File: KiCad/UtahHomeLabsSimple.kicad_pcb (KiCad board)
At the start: 2 copper layers, 20.3 x 20.3 mm, 5 parts, among them X1 SAINTCON-Minibadge-Simple

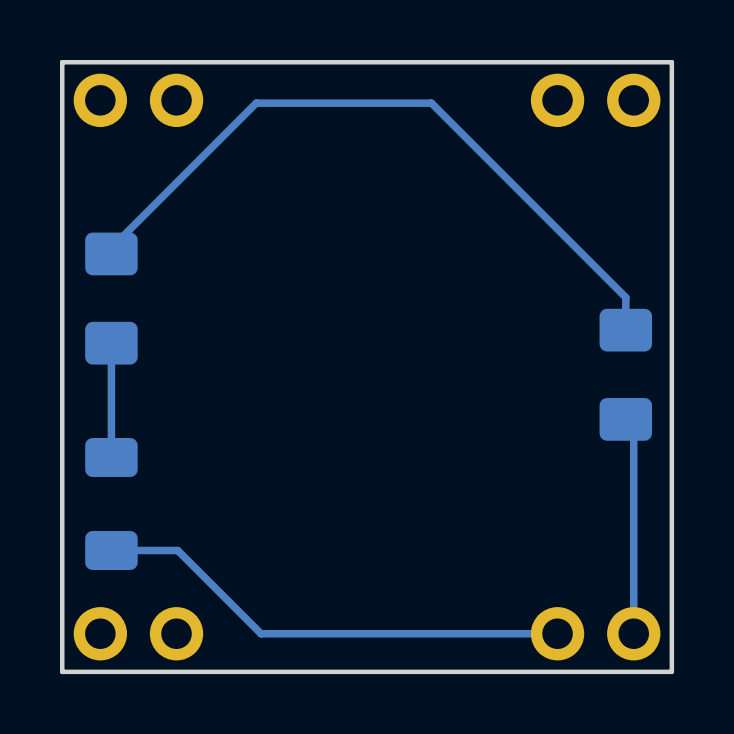
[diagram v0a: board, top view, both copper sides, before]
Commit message: Updates
Updated Schema to Parallel
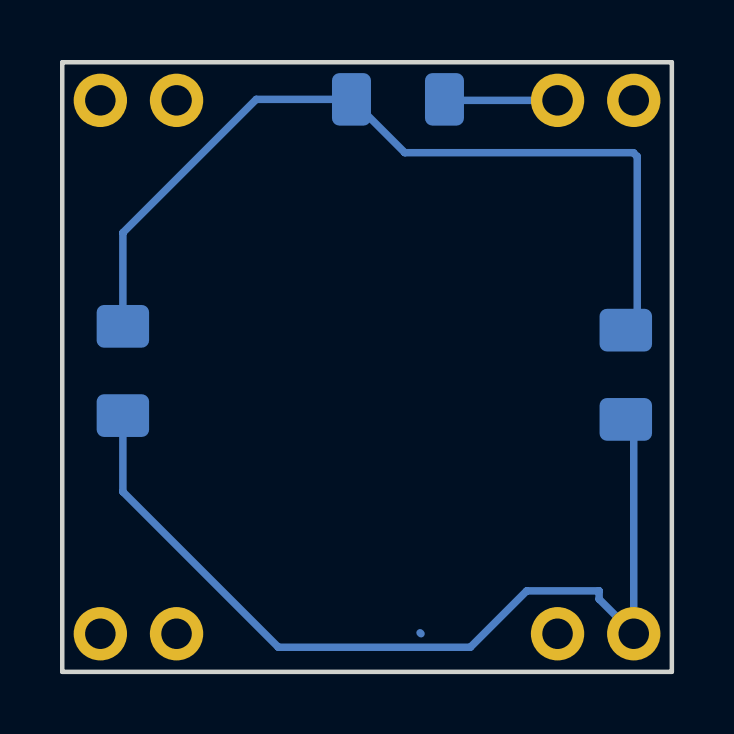
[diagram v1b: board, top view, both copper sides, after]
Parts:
- moved R1 16.5 mm to (137.2, 85.9), turned to 180 degrees
- moved D1 2.44 mm to (128.0, 94.9), turned to 90 degrees
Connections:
- D1 pad 2: Net-(D1-Pad2) -> Net-(D2-Pad2)
- D2 pad 1: Net-(X1-Pad16) -> Net-(D1-Pad1)
- D2 pad 2: Net-(D1-Pad1) -> Net-(D2-Pad2)
- R1 pad 2: Net-(D1-Pad2) -> Net-(D2-Pad2)
- X1 pad 15: Net-(R1-Pad1) -> unconnected-(X1-Pad15)
- X1 pad 16: Net-(X1-Pad16) -> Net-(D1-Pad1)
- X1 pad 7: unconnected-(X1-Pad7) -> Net-(R1-Pad1)
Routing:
- net Net-(D2-Pad2): track 0.00 -> 28.8 mm
- net Net-(R1-Pad1): track 16.0 -> 3.78 mm
- net Net-(D1-Pad1): track 23.1 -> 30.5 mm
- net Net-(X1-Pad16): track 7.25 -> 0.00 mm
- net Net-(D1-Pad2): track 3.81 -> 0.00 mm

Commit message: Re-did traces
Traces re-done
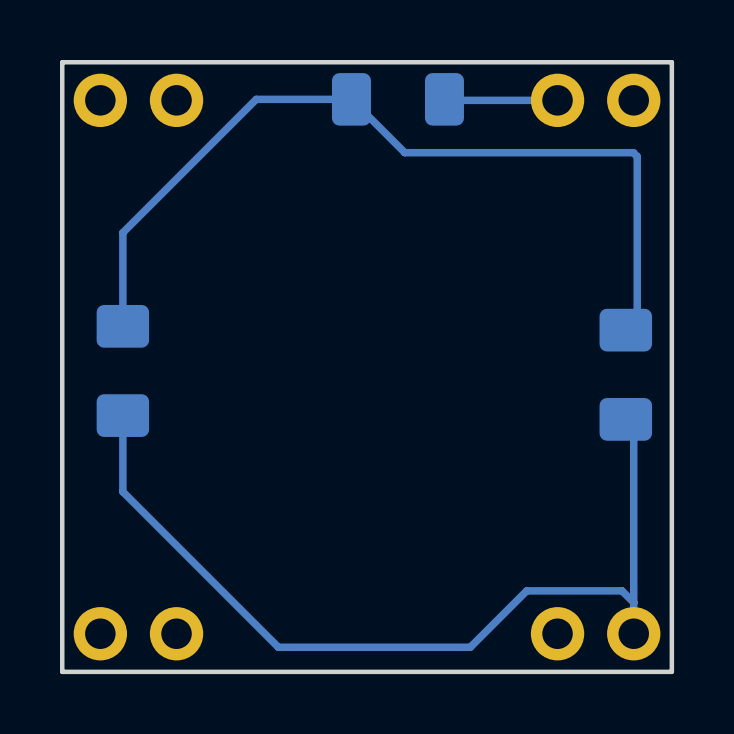
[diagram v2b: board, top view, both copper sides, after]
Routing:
- net Net-(D1-Pad1): track 30.5 -> 29.9 mm
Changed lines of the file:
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@@
     )
   )
-  (segment (start 137.955 103.665) (end 137.922 103.632) (width 0.25) (layer "B.Cu") (net 0))
   (segment (start 133.198 104.115) (end 139.598 104.115) (width 0.25) (layer "B.Cu") (net 1))
-  (segment (start 143.891 102.235) (end 143.891 102.511) (width 0.25) (layer "B.Cu") (net 1))
+  (segment (start 141.478 102.235) (end 144.653 102.235) (width 0.25) (layer "B.Cu") (net 1))
+  (segment (start 128.016 96.393) (end 128.016 98.933) (width 0.25) (layer "B.Cu") (net 1))
+  (segment (start 145.045 102.627) (end 145.045 103.665) (width 0.25) (layer "B.Cu") (net 1))
+  (segment (start 144.653 102.235) (end 145.045 102.627) (width 0.25) (layer "B.Cu") (net 1))
+  (segment (start 144.78 96.52) (end 145.045 96.785) (width 0.25) (layer "B.Cu") (net 1))
+  (segment (start 128.016 98.933) (end 133.198 104.115) (width 0.25) (layer "B.Cu") (net 1))
   (segment (start 139.598 104.115) (end 141.478 102.235) (width 0.25) (layer "B.Cu") (net 1))
-  (segment (start 144.78 96.52) (end 145.045 96.785) (width 0.25) (layer "B.Cu") (net 1))
-  (segment (start 141.478 102.235) (end 143.891 102.235) (width 0.25) (layer "B.Cu") (net 1))
-  (segment (start 128.016 96.393) (end 128.016 98.933) (width 0.25) (layer "B.Cu") (net 1))
-  (segment (start 145.045 96.785) (end 145.045 103.665) (width 0.25) (layer "B.Cu") (net 1))
-  (segment (start 128.016 98.933) (end 133.198 104.115) (width 0.25) (layer "B.Cu") (net 1))
-  (segment (start 143.891 102.511) (end 145.045 103.665) (width 0.25) (layer "B.Cu") (net 1))
+  (segment (start 145.045 96.785) (end 145.045 102.627) (width 0.25) (layer "B.Cu") (net 1))
   (segment (start 135.636 85.852) (end 132.461 85.852) (width 0.25) (layer "B.Cu") (net 7))
   (segment (start 135.636 85.852) (end 137.414 87.63) (width 0.25) (layer "B.Cu") (net 7))

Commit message: Moved Trace labels
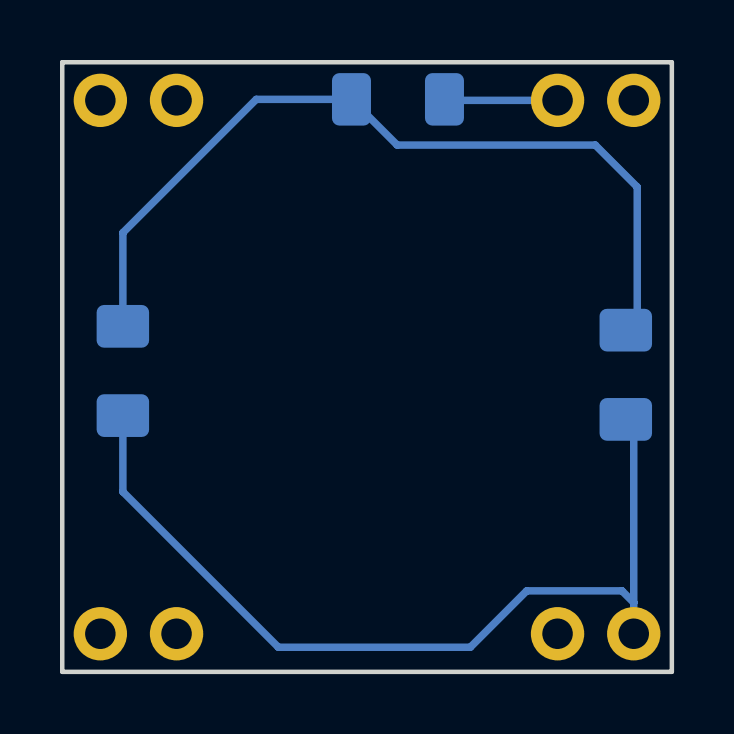
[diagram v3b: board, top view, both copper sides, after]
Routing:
- net Net-(D2-Pad2): track 28.8 -> 28.2 mm
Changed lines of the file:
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@@
     (property "Sheetname" "")
     (attr smd)
-    (fp_text reference "R1" (at 0 1.82) (layer "B.SilkS")
+    (fp_text reference "R1" (at -3.276 -0.889) (layer "B.SilkS")
       (effects (font (size 1 1) (thickness 0.15)) (justify mirror))
     )
@@
     (property "Sheetname" "")
     (attr smd)
-    (fp_text reference "D1" (at 0 1.82 90) (layer "B.SilkS")
+    (fp_text reference "D1" (at 0.9255 2.032 90) (layer "B.SilkS")
       (effects (font (size 1 1) (thickness 0.15)) (justify mirror))
     )
@@
     (property "Sheetname" "")
     (attr smd)
-    (fp_text reference "D2" (at 0 1.82 90) (layer "B.SilkS")
+    (fp_text reference "D2" (at 3.5925 -0.508 90) (layer "B.SilkS")
       (effects (font (size 1 1) (thickness 0.15)) (justify mirror))
     )
@@
   (segment (start 145.045 96.785) (end 145.045 102.627) (width 0.25) (layer "B.Cu") (net 1))
   (segment (start 135.636 85.852) (end 132.461 85.852) (width 0.25) (layer "B.Cu") (net 7))
-  (segment (start 135.636 85.852) (end 137.414 87.63) (width 0.25) (layer "B.Cu") (net 7))
-  (segment (start 145.161 87.757) (end 145.161 93.164) (width 0.25) (layer "B.Cu") (net 7))
+  (segment (start 143.764 87.376) (end 145.161 88.773) (width 0.25) (layer "B.Cu") (net 7))
+  (segment (start 145.161 93.164) (end 144.78 93.545) (width 0.25) (layer "B.Cu") (net 7))
   (segment (start 132.461 85.852) (end 128.016 90.297) (width 0.25) (layer "B.Cu") (net 7))
-  (segment (start 145.034 87.63) (end 145.161 87.757) (width 0.25) (layer "B.Cu") (net 7))
-  (segment (start 137.414 87.63) (end 145.034 87.63) (width 0.25) (layer "B.Cu") (net 7))
+  (segment (start 137.16 87.376) (end 143.764 87.376) (width 0.25) (layer "B.Cu") (net 7))
+  (segment (start 145.161 88.773) (end 145.161 93.164) (width 0.25) (layer "B.Cu") (net 7))
   (segment (start 128.016 90.297) (end 128.016 93.418) (width 0.25) (layer "B.Cu") (net 7))
-  (segment (start 145.161 93.164) (end 144.78 93.545) (width 0.25) (layer "B.Cu") (net 7))
+  (segment (start 135.636 85.852) (end 137.16 87.376) (width 0.25) (layer "B.Cu") (net 7))
   (segment (start 138.769 85.885) (end 138.736 85.852) (width 0.25) (layer "B.Cu") (net 8))
   (segment (start 142.505 85.885) (end 138.769 85.885) (width 0.25) (layer "B.Cu") (net 8))

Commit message: Fixed silkscreens / cutouts
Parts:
- removed the Ref** at (136.8, 94.7)
- added Ref**: Val**, UHLSimple_Svg, F.Cu at (136.8, 95.0)

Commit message: Updated Graphics
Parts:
- moved Ref** 0.54 mm to (136.4, 95.4)

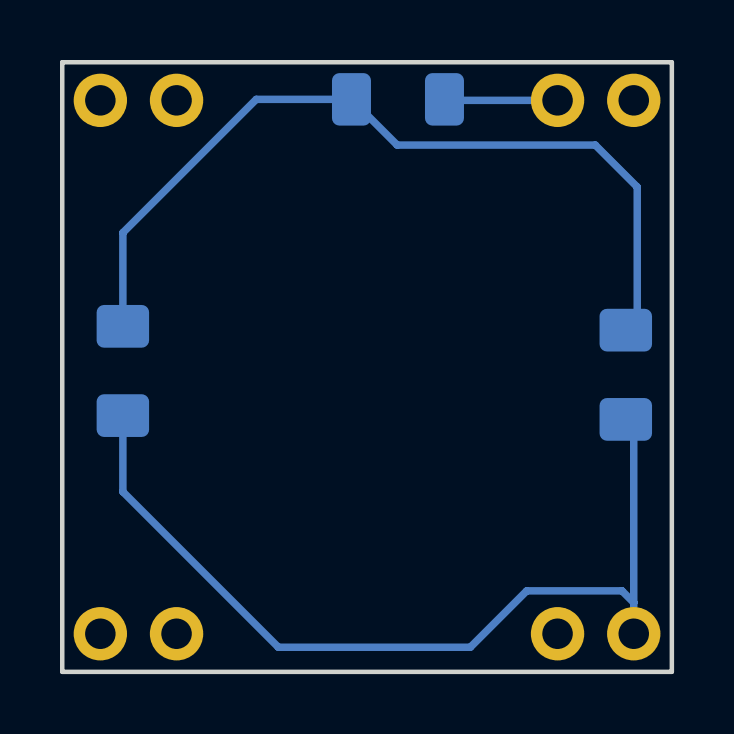
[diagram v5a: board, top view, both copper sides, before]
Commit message: Adjust labels and trace segments
Move labels into better positions.
Adjust a few of the traces.
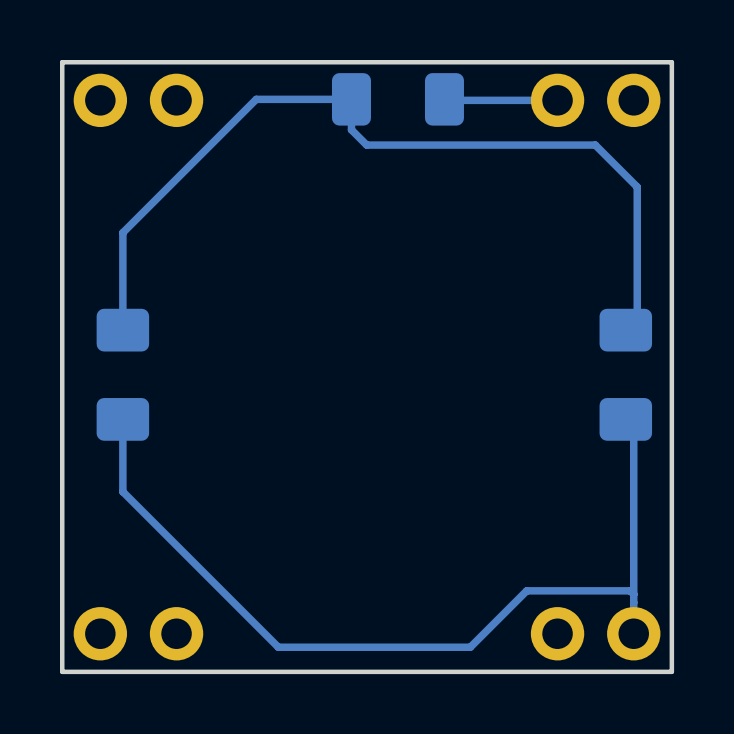
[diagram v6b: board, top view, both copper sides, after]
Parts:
- moved D1 0.13 mm to (128.0, 95.0)
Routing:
- net Net-(D2-Pad2): track 28.2 -> 29.0 mm
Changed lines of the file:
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@@
     (property "Sheetname" "")
     (attr smd)
-    (fp_text reference "R1" (at -3.276 -0.889) (layer "B.SilkS")
+    (fp_text reference "R1" (at 3.582 -0.889) (layer "B.SilkS")
       (effects (font (size 1 1) (thickness 0.15)) (justify mirror))
     )
@@
   )
   (footprint "LED_SMD:LED_1206_3216Metric_Pad1.42x1.75mm_HandSolder" (layer "B.Cu")
-    (at 128.016 94.9055 90)
+    (at 128.016 95.0325 90)
     (descr "LED SMD 1206 (3216 Metric), square (rectangular) end terminal, IPC_7351 nominal, (Body size source: http://www.tortai-tech.com/upload/download/2011102023233369053.pdf), generated with kicad-footprint-generator")
     (tags "LED handsolder")
@@
     (property "Sheetname" "")
     (attr smd)
-    (fp_text reference "D1" (at 0.9255 2.032 90) (layer "B.SilkS")
+    (fp_text reference "D1" (at 3.4655 1.016 90) (layer "B.SilkS")
       (effects (font (size 1 1) (thickness 0.15)) (justify mirror))
     )
@@
     (property "Sheetname" "")
     (attr smd)
-    (fp_text reference "D2" (at 3.5925 -0.508 90) (layer "B.SilkS")
+    (fp_text reference "D2" (at 3.5925 -1.016 90) (layer "B.SilkS")
       (effects (font (size 1 1) (thickness 0.15)) (justify mirror))
     )
@@
     )
   )
+  (segment (start 128.016 98.933) (end 128.016 96.52) (width 0.25) (layer "B.Cu") (net 1))
   (segment (start 133.198 104.115) (end 139.598 104.115) (width 0.25) (layer "B.Cu") (net 1))
-  (segment (start 141.478 102.235) (end 144.653 102.235) (width 0.25) (layer "B.Cu") (net 1))
-  (segment (start 128.016 96.393) (end 128.016 98.933) (width 0.25) (layer "B.Cu") (net 1))
+  (segment (start 144.929 102.235) (end 145.045 102.351) (width 0.25) (layer "B.Cu") (net 1))
   (segment (start 145.045 102.627) (end 145.045 103.665) (width 0.25) (layer "B.Cu") (net 1))
-  (segment (start 144.653 102.235) (end 145.045 102.627) (width 0.25) (layer "B.Cu") (net 1))
   (segment (start 144.78 96.52) (end 145.045 96.785) (width 0.25) (layer "B.Cu") (net 1))
+  (segment (start 145.045 102.351) (end 145.045 102.627) (width 0.25) (layer "B.Cu") (net 1))
   (segment (start 128.016 98.933) (end 133.198 104.115) (width 0.25) (layer "B.Cu") (net 1))
   (segment (start 139.598 104.115) (end 141.478 102.235) (width 0.25) (layer "B.Cu") (net 1))
-  (segment (start 145.045 96.785) (end 145.045 102.627) (width 0.25) (layer "B.Cu") (net 1))
-  (segment (start 135.636 85.852) (end 132.461 85.852) (width 0.25) (layer "B.Cu") (net 7))
-  (segment (start 143.764 87.376) (end 145.161 88.773) (width 0.25) (layer "B.Cu") (net 7))
-  (segment (start 145.161 93.164) (end 144.78 93.545) (width 0.25) (layer "B.Cu") (net 7))
-  (segment (start 132.461 85.852) (end 128.016 90.297) (width 0.25) (layer "B.Cu") (net 7))
-  (segment (start 137.16 87.376) (end 143.764 87.376) (width 0.25) (layer "B.Cu") (net 7))
-  (segment (start 145.161 88.773) (end 145.161 93.164) (width 0.25) (layer "B.Cu") (net 7))
-  (segment (start 128.016 90.297) (end 128.016 93.418) (width 0.25) (layer "B.Cu") (net 7))
-  (segment (start 135.636 85.852) (end 137.16 87.376) (width 0.25) (layer "B.Cu") (net 7))
+  (segment (start 141.478 102.235) (end 144.929 102.235) (width 0.25) (layer "B.Cu") (net 1))
+  (segment (start 145.045 96.785) (end 145.045 102.351) (width 0.25) (layer "B.Cu") (net 1))
+  (segment (start 136.144 87.376) (end 135.636 86.868) (width 0.25) (layer "B.Cu") (net 7))
+  (segment (start 128.016 93.545) (end 128.016 90.297) (width 0.25) (layer "B.Cu") (net 7))
+  (segment (start 132.461 85.852) (end 135.636 85.852) (width 0.25) (layer "B.Cu") (net 7))
+  (segment (start 144.78 93.545) (end 145.161 93.164) (width 0.25) (layer "B.Cu") (net 7))
+  (segment (start 145.161 93.164) (end 145.161 88.773) (width 0.25) (layer "B.Cu") (net 7))
+  (segment (start 145.161 88.773) (end 143.764 87.376) (width 0.25) (layer "B.Cu") (net 7))
+  (segment (start 135.636 86.868) (end 135.636 85.852) (width 0.25) (layer "B.Cu") (net 7))
+  (segment (start 128.016 90.297) (end 132.461 85.852) (width 0.25) (layer "B.Cu") (net 7))
+  (segment (start 143.764 87.376) (end 136.144 87.376) (width 0.25) (layer "B.Cu") (net 7))
   (segment (start 138.769 85.885) (end 138.736 85.852) (width 0.25) (layer "B.Cu") (net 8))
   (segment (start 142.505 85.885) (end 138.769 85.885) (width 0.25) (layer "B.Cu") (net 8))
